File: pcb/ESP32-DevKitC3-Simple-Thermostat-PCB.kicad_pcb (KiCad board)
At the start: 4 copper layers, 133 x 89.5 mm, 60 parts, among them J1 PINHD_1x18_Male, J2 Screw_Terminal_9_P3.50mm, J3 DS18B20, J4 3.2 lcd tft, J5 AHT20 Board, J6 LD2410C, K1 G5Q-1A, K2 G5Q-1A, K3 G5Q-1A, K4 G5Q-1A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

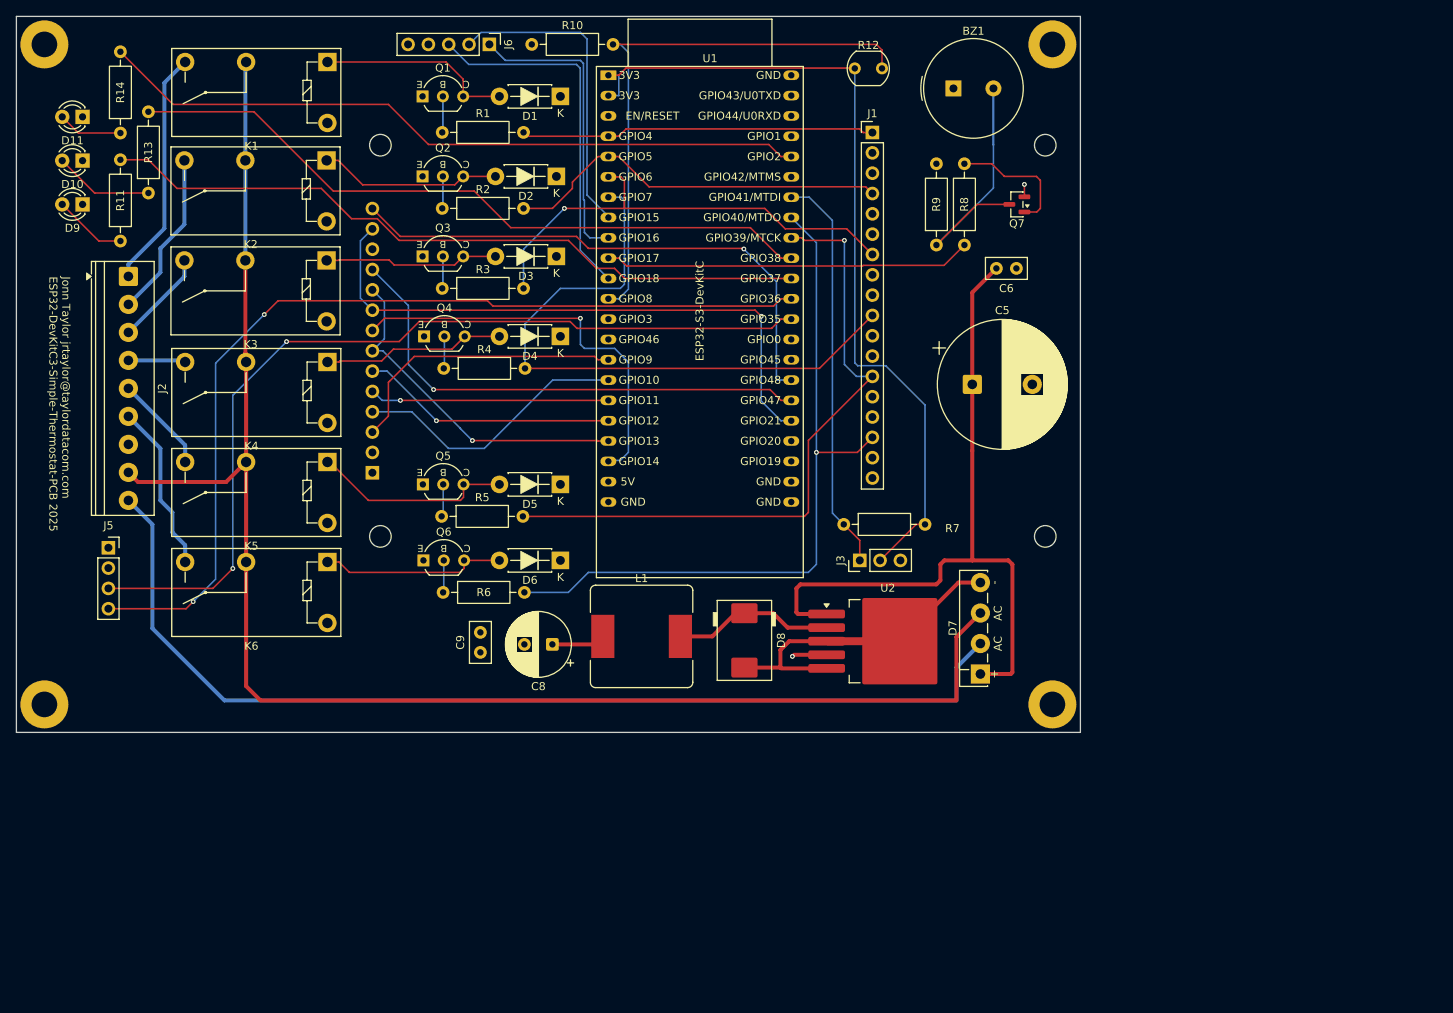
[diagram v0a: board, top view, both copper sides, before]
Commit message: add relay common and split c input
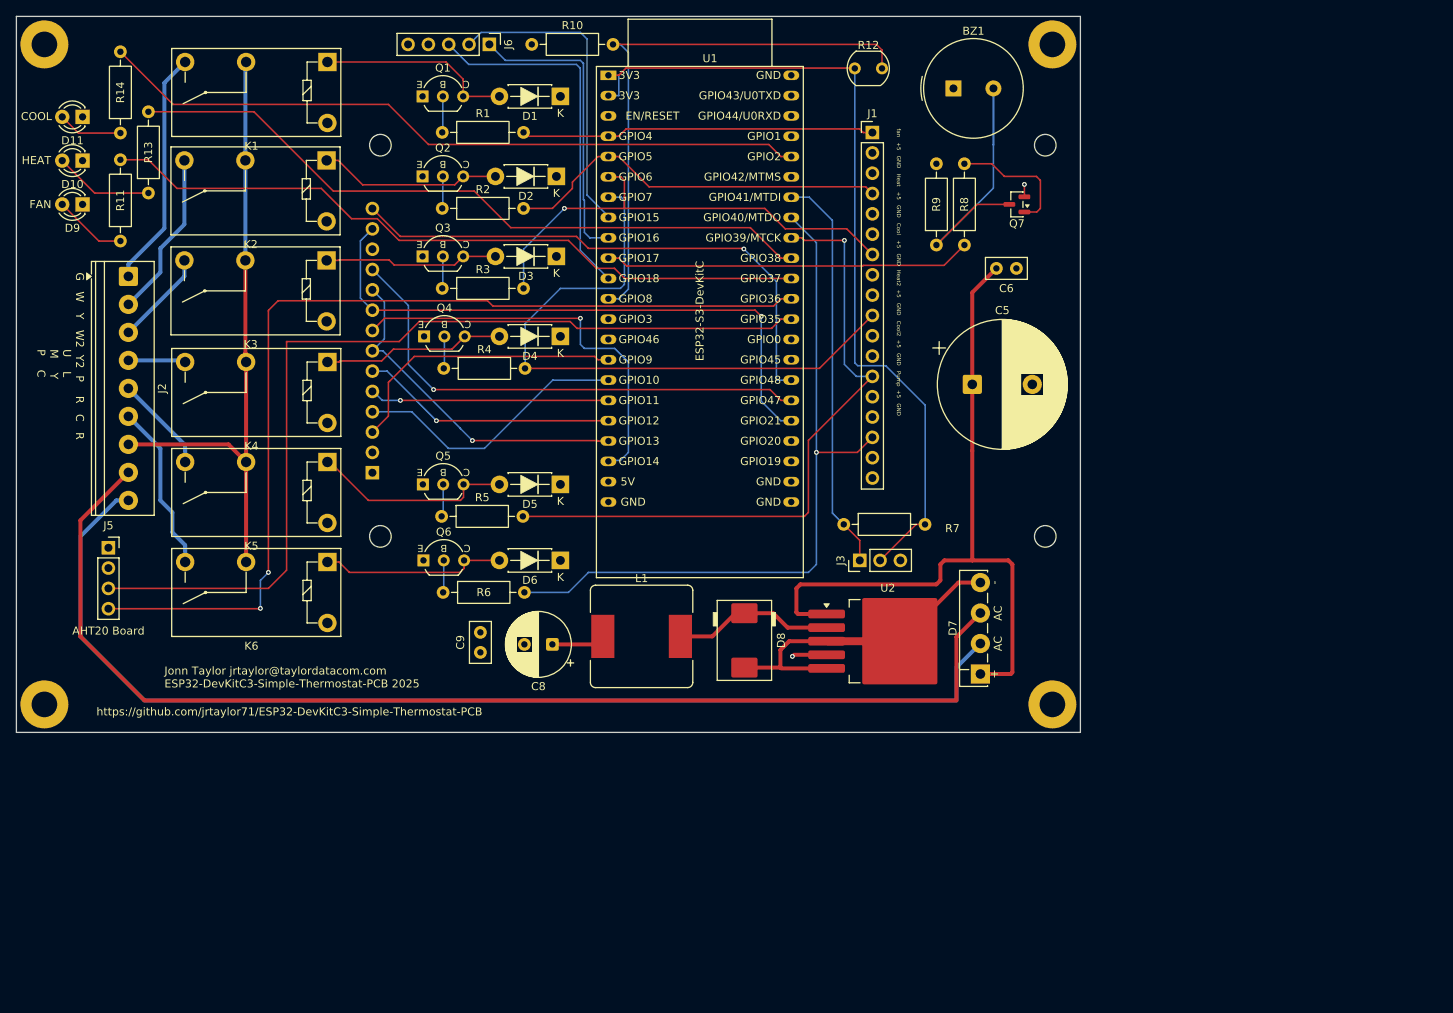
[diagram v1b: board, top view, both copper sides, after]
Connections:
- J1 pad 6: unconnected-(J1-Pad6) -> GND
- J2 pad 7: unconnected-(J2-Pad7) -> RLY-C
- K1 pad 2: VAC-C -> RLY-C
- K2 pad 2: VAC-C -> RLY-C
- K3 pad 2: VAC-C -> RLY-C
- K4 pad 2: VAC-C -> RLY-C
- K5 pad 2: VAC-C -> RLY-C
- K6 pad 2: VAC-C -> RLY-C
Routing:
- net RLY-C: track 0.00 -> 78.2 mm
- net VAC-C: track 196.0 -> 148.0 mm
- net VAC-R: track 129.8 -> 141.5 mm
- net SDA: track 117.8 -> 123.2 mm
- net SCL: track 112.7 -> 116.8 mm, vias 2 -> 0
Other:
- board text added: "G W Y W2 Y2 P R C R U L M Y P C"
- board text added: "fan +5 GND Heat +5 GND Cool +5 GND Heat2 +5 GND Cool2 +5 GND Pump +5 GND"
- board text added: "https://github.com/jrtaylor71/ESP32-DevKitC3-Simple-Thermostat-PCB"

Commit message: Update PCB design and regenerate gerber files
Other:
- board text added: "Version: 1.0"
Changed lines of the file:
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@@
+		)
+	)
+	(gr_text "Version: 1.0"
+		(at 65 105 0)
+		(layer "F.SilkS")
+		(effects
+			(font
+				(size 1 1)
+				(thickness 0.1)
+			)
+			(justify left bottom)
 		)
 	)

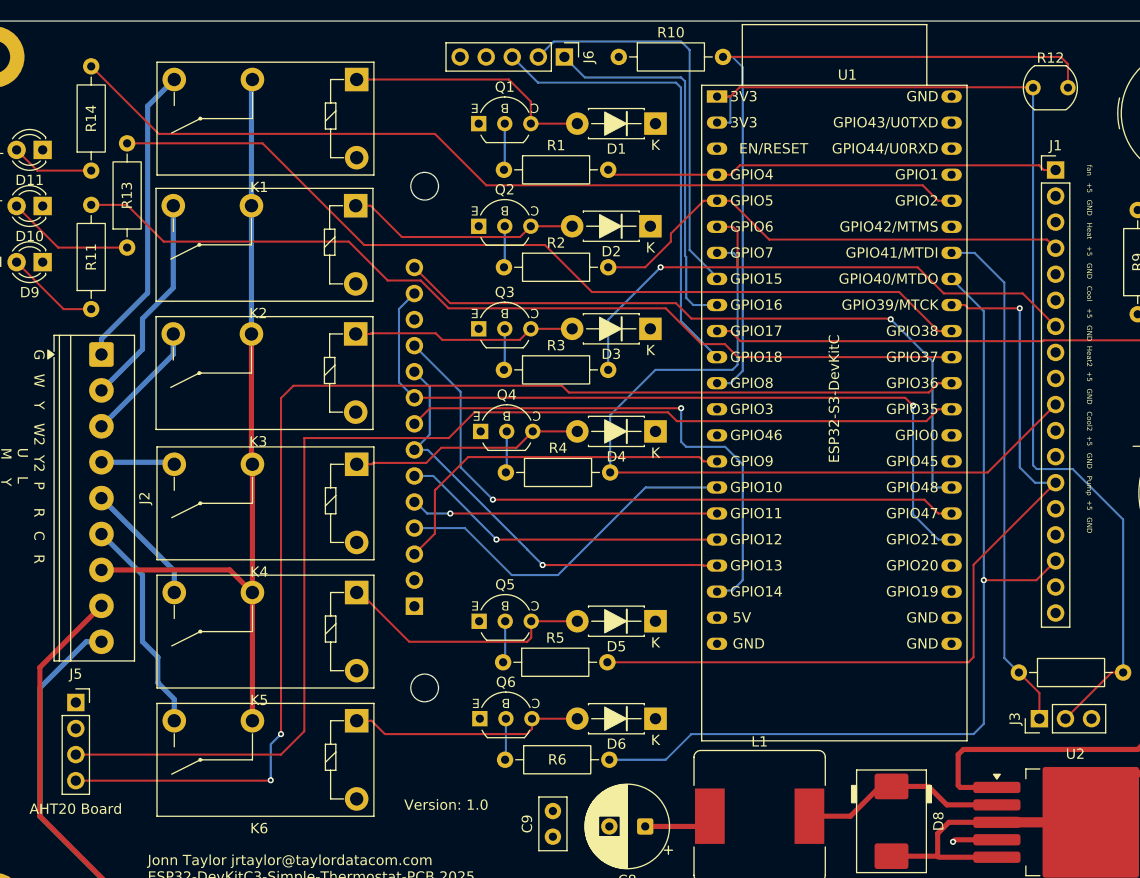
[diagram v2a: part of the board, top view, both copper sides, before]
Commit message: Update PCB design with latest revisions
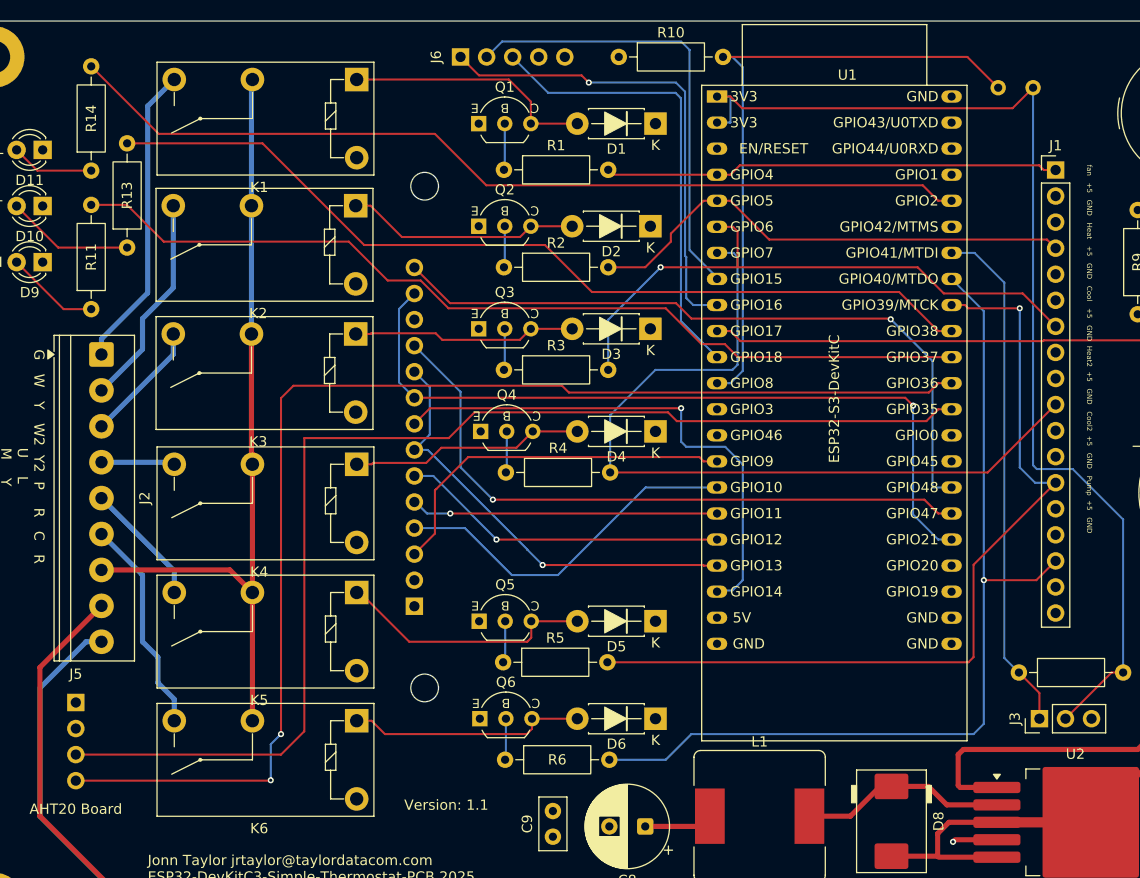
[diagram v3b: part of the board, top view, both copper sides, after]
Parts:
- J5, J6, R12: moved to B.Cu
- moved J6 10.1 mm to (70.5, 31.5)
- turned J5 to 180 degrees
- turned R12 to 180 degrees
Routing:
- net LD_TX: track 37.2 -> 46.7 mm, vias 0 -> 1
- net LIGHT_SENS: track 71.1 -> 63.0 mm
- net LD_RX: track 39.1 -> 44.2 mm
- net 3.3V: track 106.5 -> 107.4 mm
- net MOTION: track 45.4 -> 44.8 mm
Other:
- board text added: "Version: 1.1"
- board text removed: "Version: 1.0"

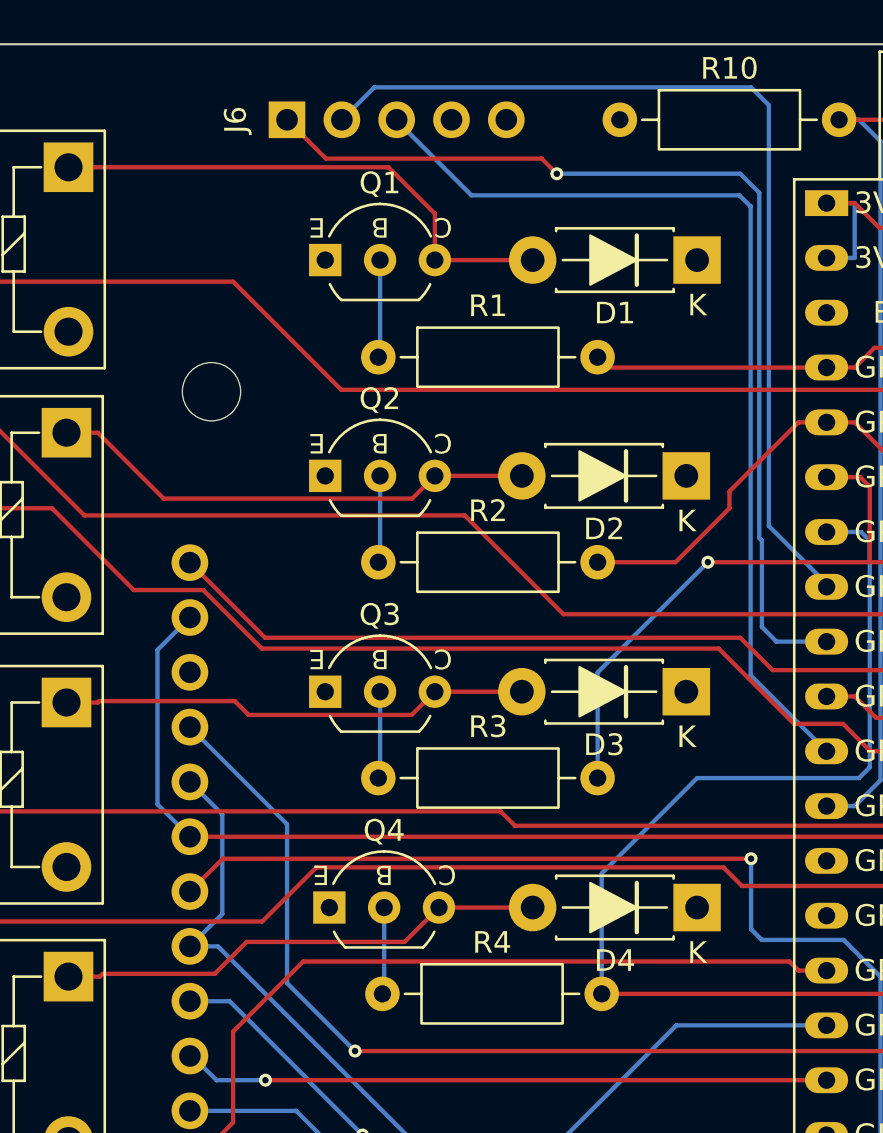
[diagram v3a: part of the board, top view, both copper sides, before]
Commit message: Bump version to 1.3.7 - Fix fan relay oscillation bug when manual 'on' mode conflicts with HVAC fan control. Update schermatic and PCB for missing trace.
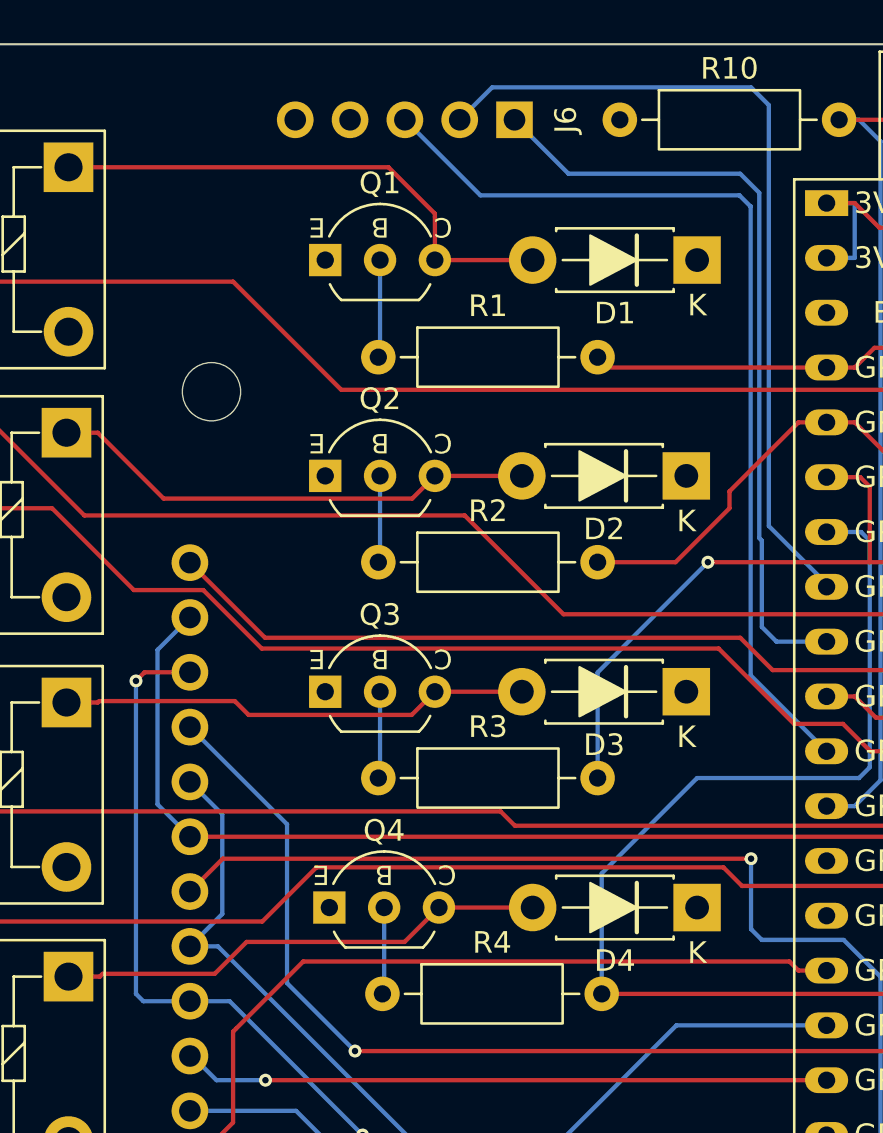
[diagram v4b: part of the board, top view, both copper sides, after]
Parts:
- moved J6 10.5 mm to (81.0, 31.5), turned to 90 degrees
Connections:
- J4 pad 12: MOSI_23 -> MOSI_12
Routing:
- net MOSI_12: track 32.1 -> 51.9 mm, vias 1 -> 2
- net LD_TX: track 46.7 -> 36.2 mm, vias 1 -> 0
- net LD_RX: track 44.2 -> 38.7 mm

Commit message: Cleanup old files.
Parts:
- added J7: PINHD_1x3_Male, Connector_PinHeader_2.54mm:PinHeader_1x03_P2.54mm_Vertical, F.Cu at (37.8, 108.1)
- J5: value AHT20 Board -> I2C Sensor
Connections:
- J5 pad 1: +5V -> Net-(J5-Pad1)
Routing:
- net 3.3V: track 107.4 -> 200.1 mm
- net GND: track 42.6 -> 88.3 mm, vias 1 -> 8
- net Net-(J5-Pad1): track 0.00 -> 19.5 mm
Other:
- board text added: "Version: 1.2"
- board text removed: "Version: 1.1"
